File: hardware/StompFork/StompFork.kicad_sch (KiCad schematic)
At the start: 0 parts

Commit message: Create sketch using unity buffers
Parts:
- added C1, C3: 100nF, symbol Device:C
- added C10, C11, C12, C9: 47pF, symbol Device:C
- added C2: 100uF, symbol Device:C_Polarized
- added C4: 47uF, symbol Device:C_Polarized
- added C5: 1uF (poly), symbol Device:C_Polarized
- added C6, C7, C8: 22uF, symbol Device:C_Polarized
- added J1: Conn_01x02_Socket, symbol Connector:Conn_01x02_Socket
- added J2: Input, symbol Connector_Audio:AudioJack2
- added J3: Direct Output, symbol Connector_Audio:AudioJack2
- added J4: Buffered Output 1, symbol Connector_Audio:AudioJack2
- added J5: Buffered Output 2, symbol Connector_Audio:AudioJack2
- added R1, R2: 10k, symbol Device:R
- added R3: 1M, symbol Device:R
- added R4, R6, R8: 100, symbol Device:R
- added R5, R7, R9: 100k, symbol Device:R
- added RV1, RV2: 10k, symbol Device:R_Potentiometer
- added U1: TL074, Package_DIP:DIP-14_W7.62mm_Socket, symbol Amplifier_Operational:TL074
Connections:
- new net: C5.1, R3.2, U1.5 (+)
- new net: C5.2, J2.T
- new net: C12.1, C12.2, R8.1, U1.13 (-), U1.14
- new net: C10.1, C10.2, R4.1, RV1.1, RV2.1, U1.6 (-), U1.7
- new net: C6.1, R4.2
- new net: C8.2, J5.T, R9.2
- new net: C3.1, C4.1, R1.2, R2.1, U1.3 (+)
- new net: C8.1, R8.2
- new net: C7.2, J4.T, R7.2
- new net: C6.2, J3.T, R5.2
- new net: RV2.2, U1.12 (+)
- new net: C11.1, C11.2, R6.1, U1.8, U1.9 (-)
- new net: RV1.2, U1.10 (+)
- new net: C7.1, R6.2
- new net GND: C1.2, C2.2, C3.2, C4.2, J1.2 (Pin_2), J2.S, J3.S, J4.S, J5.S, R2.2, R5.1, R7.1, R9.1, U1.11 (V-)
- new net VCC: C1.1, C2.1, J1.1 (Pin_1), R1.1, U1.4 (V+)
- new net VREF: C9.1, C9.2, R3.1, RV1.3, RV2.3, U1.1, U1.2 (-)

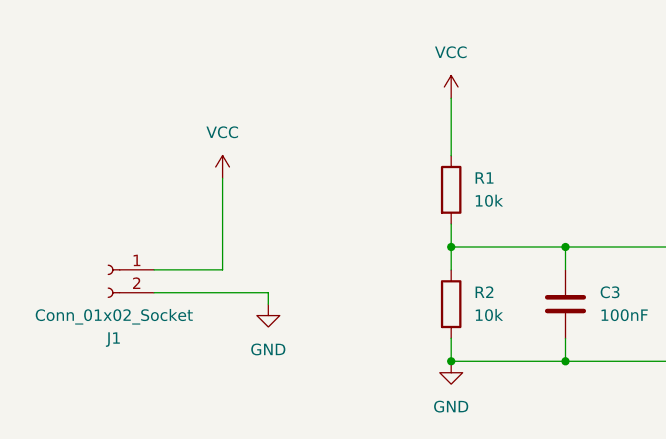
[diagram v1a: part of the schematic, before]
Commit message: Add protection diode
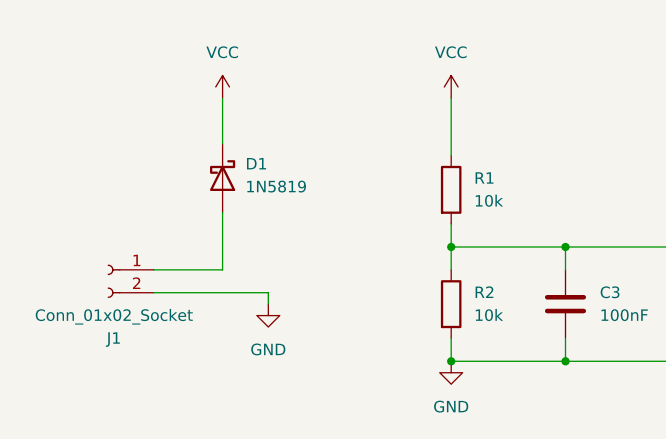
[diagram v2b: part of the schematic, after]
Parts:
- added D1: 1N5819, Diode_THT:D_DO-41_SOD81_P10.16mm_Horizontal, symbol Diode:1N5819
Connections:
- net VCC: now also D1.1 (K); no longer J1.1 (Pin_1)
- new net: D1.2 (A), J1.1 (Pin_1)
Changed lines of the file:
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@@
-	(wire
-		(pts
-			(xy 38.1 30.48) (xy 38.1 40.64)
-		)
-		(stroke
-			(width 0)
-			(type default)
-		)
-	)
 	(wire
 		(pts
@@
 	(wire
 		(pts
+			(xy 38.1 21.59) (xy 38.1 26.67)
+		)
+		(stroke
+			(width 0)
+			(type default)
+		)
+	)
+	(wire
+		(pts
 			(xy 251.46 135.89) (xy 251.46 138.43)
 		)
@@
 		(pts
 			(xy 187.96 39.37) (xy 171.45 39.37)
+		)
+		(stroke
+			(width 0)
+			(type default)
+		)
+	)
+	(wire
+		(pts
+			(xy 38.1 34.29) (xy 38.1 40.64)
 		)
 		(stroke
@@
 	(symbol
 		(lib_id "power:VCC")
-		(at 38.1 30.48 0)
+		(at 38.1 21.59 0)
 		(unit 1)
 		(exclude_from_sim no)
@@
 		(fields_autoplaced yes)
 		(property "Reference" "#PWR02"
-			(at 38.1 34.29 0)
+			(at 38.1 25.4 0)
 			(effects
 				(font
@@
 		)
 		(property "Value" "VCC"
-			(at 38.1 25.4 0)
+			(at 38.1 16.51 0)
 			(effects
 				(font
@@
 		)
 		(property "Footprint" ""
-			(at 38.1 30.48 0)
+			(at 38.1 21.59 0)
 			(effects
 				(font
@@
 		)
 		(property "Datasheet" ""
-			(at 38.1 30.48 0)
+			(at 38.1 21.59 0)
 			(effects
 				(font
@@
 		)
 		(property "Description" "Power symbol creates a global label with name \"VCC\""
-			(at 38.1 30.48 0)
+			(at 38.1 21.59 0)
 			(effects
 				(font
@@
 					(unit 1)
 				)
+			)
+		)
+	)
+	(symbol
+		(lib_id "Diode:1N5819")
+		(at 38.1 30.48 270)
+		(unit 1)
+		(exclude_from_sim no)
+		(in_bom yes)
+		(on_board yes)
+		(dnp no)
+		(fields_autoplaced yes)
+		(property "Reference" "D1"
+			(at 40.64 28.8924 90)
+			(effects
+				(font
+					(size 1.27 1.27)
+				)
+				(justify left)
+			)
+		)
+		(property "Value" "1N5819"
+			(at 40.64 31.4324 90)
+			(effects
+				(font
+					(size 1.27 1.27)
+				)
+				(justify left)
+			)
+		)
+		(property "Footprint" "Diode_THT:D_DO-41_SOD81_P10.16mm_Horizontal"
+			(at 33.655 30.48 0)
+			(effects
+				(font
+					(size 1.27 1.27)
+				)
+				(hide yes)
+			)
+		)
+		(property "Datasheet" "http://www.vishay.com/docs/88525/1n5817.pdf"
+			(at 38.1 30.48 0)
+			(effects
+				(font
+					(size 1.27 1.27)
+				)
+				(hide yes)
+			)
+		)
+		(property "Description" "40V 1A Schottky Barrier Rectifier Diode, DO-41"
+			(at 38.1 30.48 0)
+			(effects
+				(font
+					(size 1.27 1.27)
+				)
+				(hide yes)
+			)
+		)
+		(pin "1"
+		)
+		(pin "2"
+		)
+		(instances
+			(project ""
+				(path "/9aeb4a2f-ec41-41a2-8cef-c6517b2f11ba"
+					(reference "D1")
+					(unit 1)
+				)

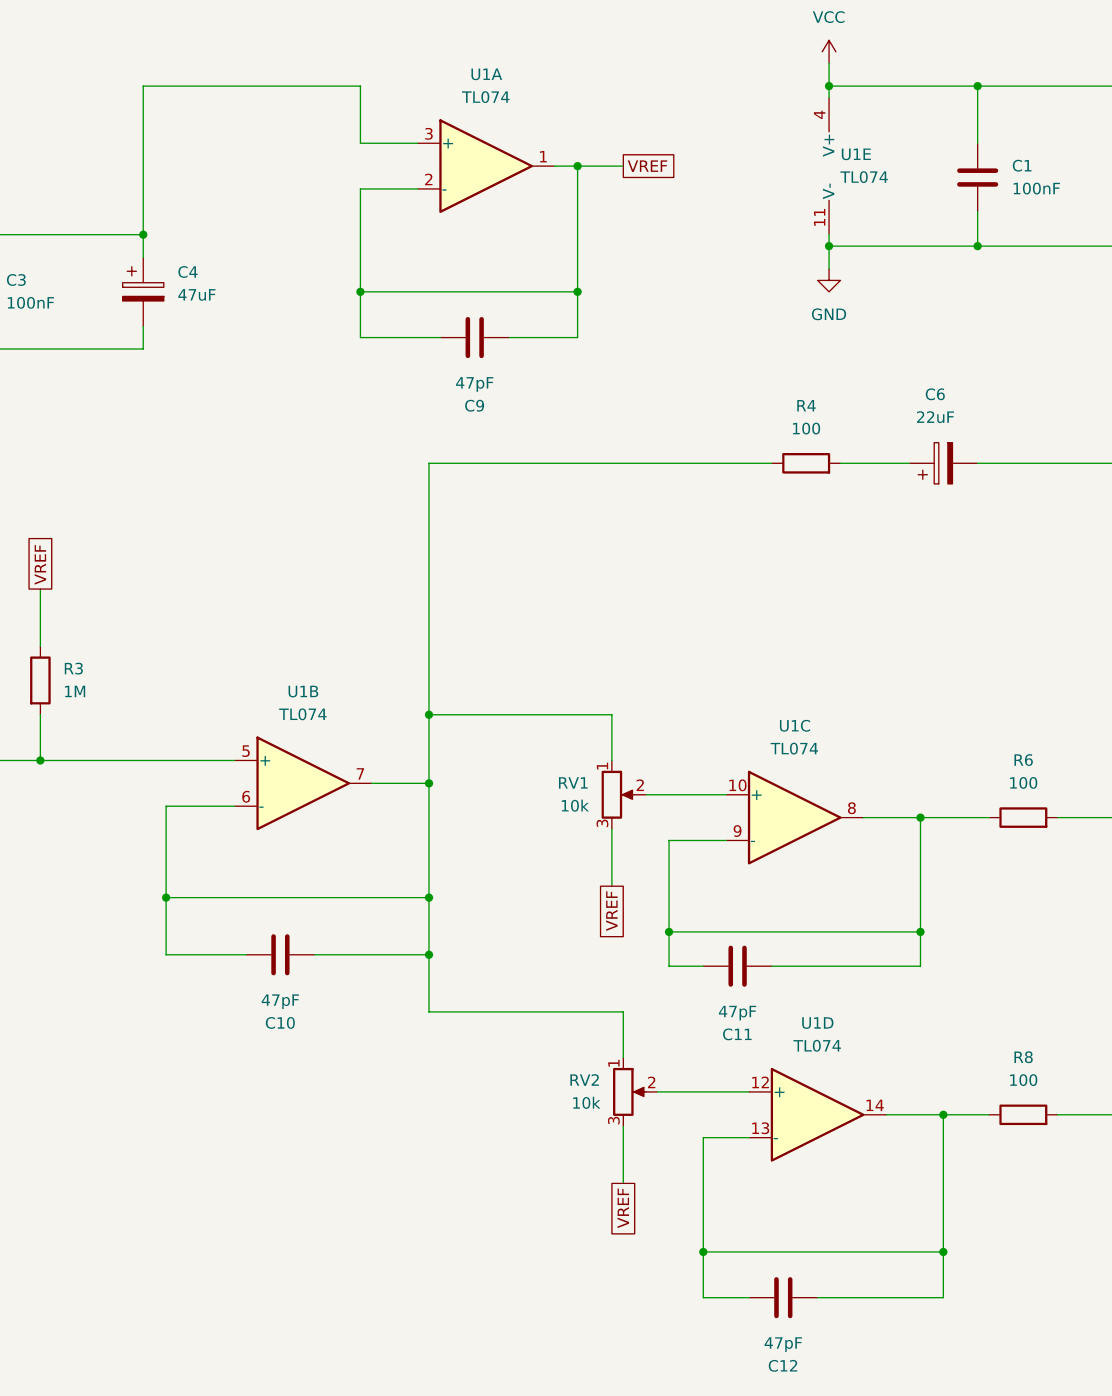
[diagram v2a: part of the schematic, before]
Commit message: Fix feedback paths
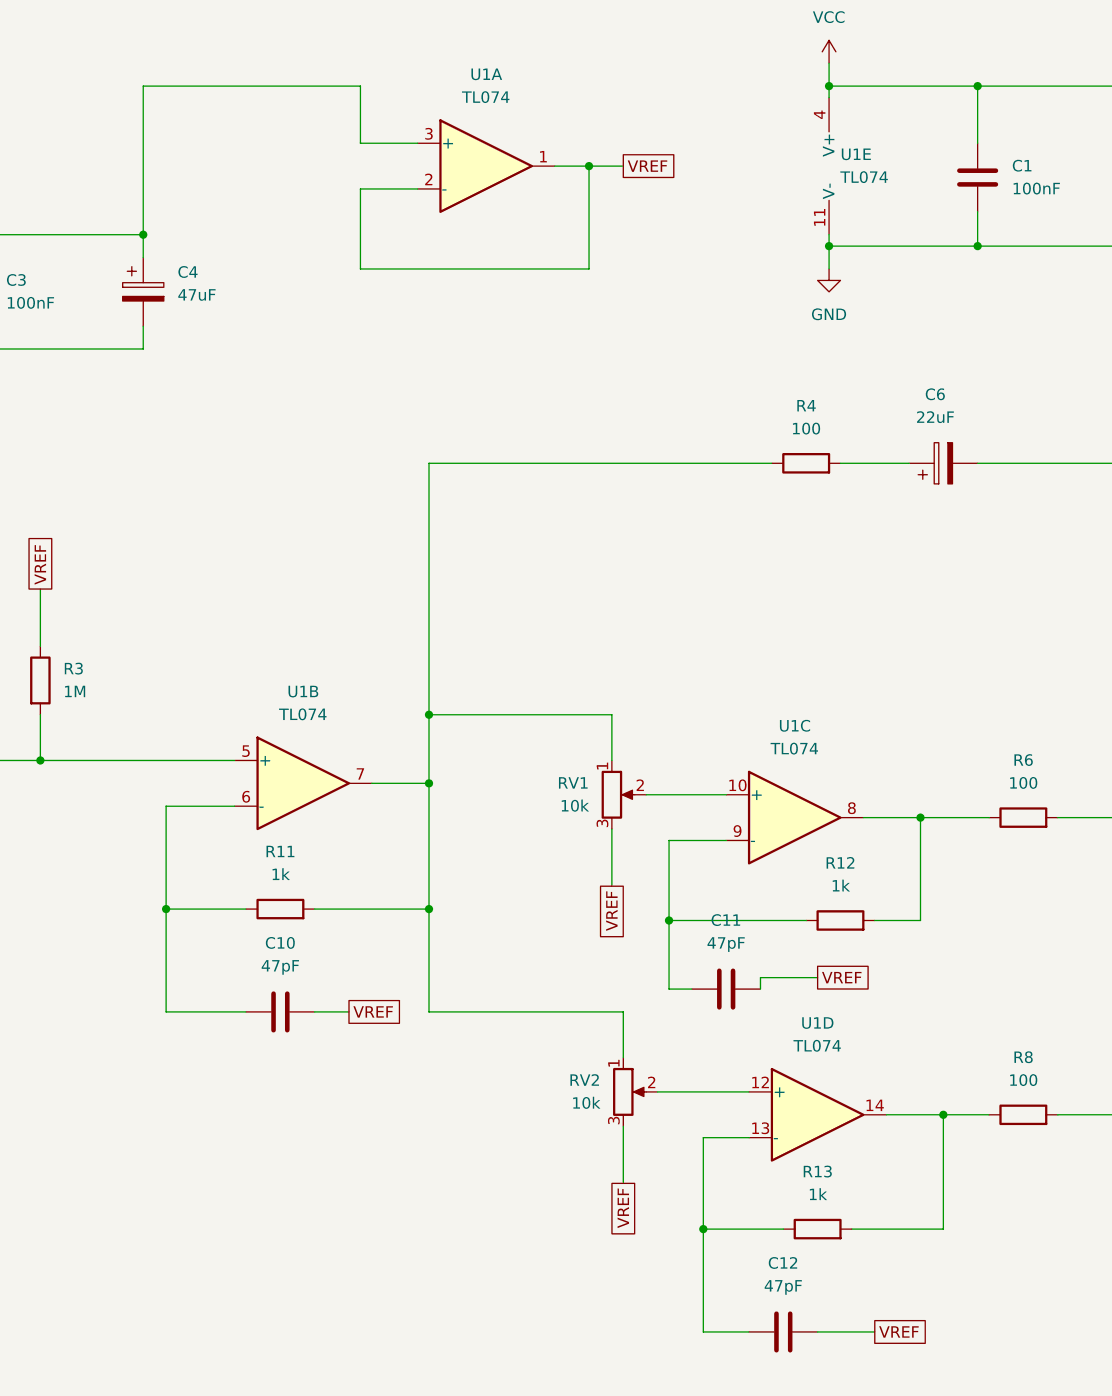
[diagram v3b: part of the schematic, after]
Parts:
- removed C9: 47pF, symbol Device:C
- added R11, R12, R13: 1k, symbol Device:R
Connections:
- net VREF: now also C10.2, C11.2, C12.2
- net at R4.1, RV1.1, RV2.1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: now also R11.2; no longer C10.1, C10.2, U1.6 (-)
- new net: C12.1, R13.1, U1.13 (-)
- new net: R13.2, R8.1, U1.14
- new net: C10.1, R11.1, U1.6 (-)
- new net: C11.1, R12.1, U1.9 (-)
- new net: R12.2, R6.1, U1.8
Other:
- moved on the sheet: C10, C11, C12

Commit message: Polish schematic
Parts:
- removed C4: 47uF, symbol Device:C_Polarized
- added C2: 47uF, symbol Device:C_Polarized
- C5: value 1uF (poly) -> 1uF
- J1: value Conn_01x02_Socket -> Power
- renumbered C3 to C1, C1 to C3, C2 to C4, R11 to R10, R12 to R11, R13 to R12
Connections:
- net GND: now also C2.2
- net at C1.1, R1.2, R2.1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: now also C2.1
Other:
- moved on the sheet: C1, C10, C11, C12, C3, C4, C5, C6, C7, C8, D1, J1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

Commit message: Update specs
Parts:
- J4: value Buffered Output 1 -> Stompbox Output 1
- J5: value Buffered Output 2 -> Stompbox Output 2
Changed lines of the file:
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@@
 			)
 		)
-		(property "Description" "Electrolytic or Polypropylene"
-			(at 51.816 30.48 90)
+		(property "Description" "Electrolytic or Film (PP/MKT)"
+			(at 52.324 30.734 90)
 			(effects
 				(font
@@
 			)
 		)
-		(property "Value" "Buffered Output 2"
+		(property "Value" "Stompbox Output 2"
 			(at 272.415 124.46 0)
 			(effects
@@
 			)
 		)
-		(property "Value" "Buffered Output 1"
+		(property "Value" "Stompbox Output 1"
 			(at 272.415 92.71 0)
 			(effects

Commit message: Update specs
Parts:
- J2: value Input -> Line-Level Input
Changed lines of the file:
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@@
 			)
 		)
-		(property "Value" "Input"
+		(property "Value" "Line-Level Input"
 			(at 26.035 48.26 0)
 			(effects
